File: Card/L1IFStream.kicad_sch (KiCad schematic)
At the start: 109 parts, among them J1 Conn_Coaxial, J2 USB_A, J3 RF_Shield_One_Piece, J4 Conn_Coaxial, U1 MAX2769BETI+T, U10 74LVC374, U11 74HC2GU04, U2 TPS717285DCK, U3 TPS717285DCK, U4 NCP164, U5 93LC66BT-I_OT, U6 FT2232H-Interface_USB, U7 74LVC1G74, U8 74LVC1G04, U9 74LVC374, X1 SIT5156, X2 SiT2024B, X3 QPQ1060

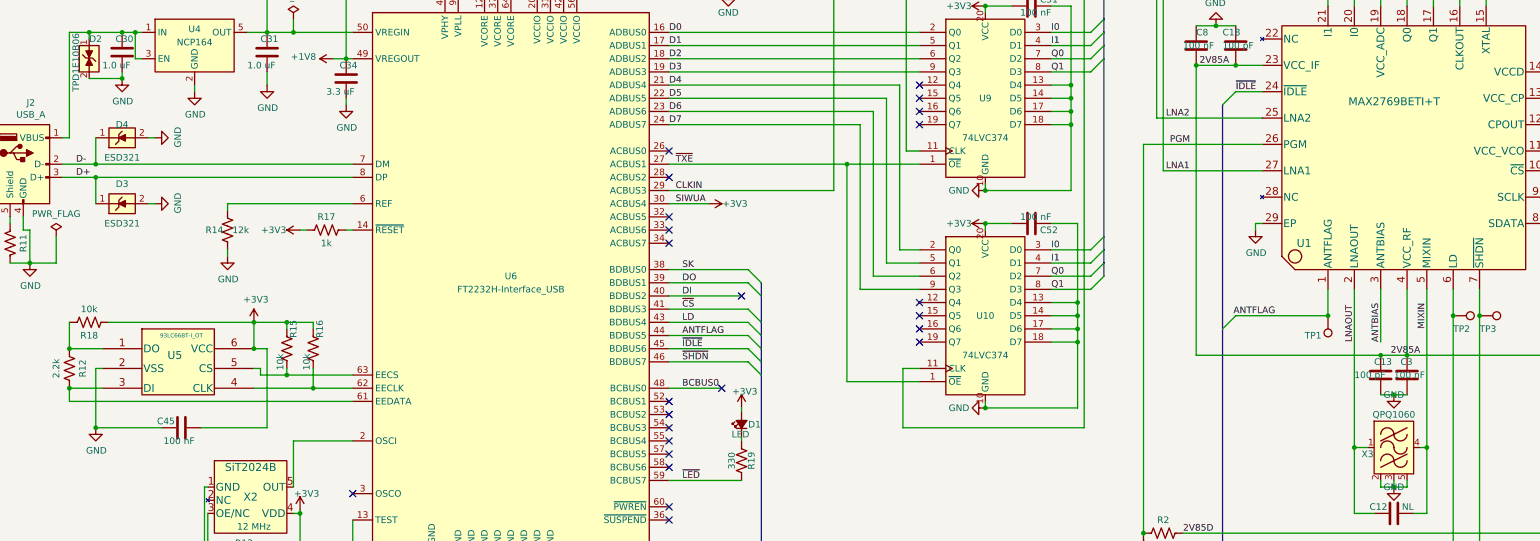
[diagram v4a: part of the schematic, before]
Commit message: Added SiTime 5156 16.367667 oscillator as alternate.
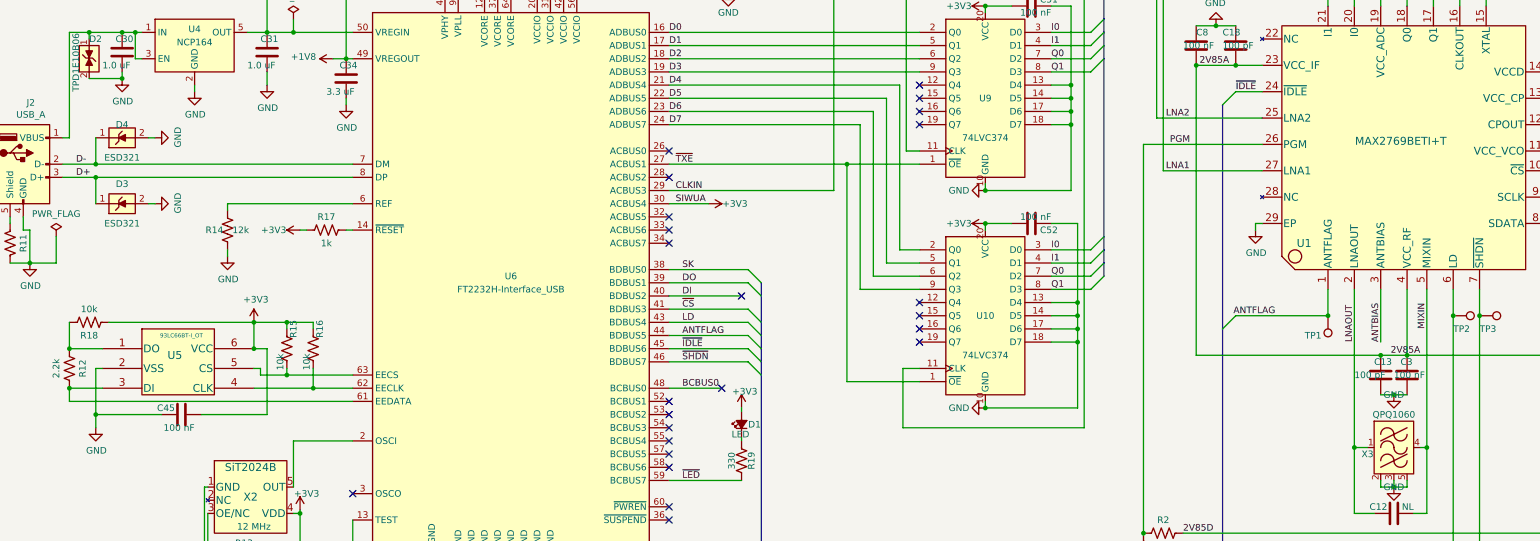
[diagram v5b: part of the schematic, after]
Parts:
- X1: MPN2 (none) -> SIT5156AICFK-30NO-16.367667; VPN2 (none) -> 1473-SIT5156AICFK-30N0-16.367667-ND
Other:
- moved on the sheet: C45
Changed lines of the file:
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@@
   (junction (at 29.21 123.19) (diameter 0) (color 0 0 0 0)
   )
-  (junction (at 34.29 138.43) (diameter 0) (color 0 0 0 0)
-  )
   (junction (at 401.32 139.7) (diameter 0) (color 0 0 0 0)
   )
@@
   (junction (at 223.52 22.86) (diameter 0) (color 0 0 0 0)
   )
+  (junction (at 34.29 135.89) (diameter 0) (color 0 0 0 0)
+  )
   (junction (at 82.55 67.31) (diameter 0) (color 0 0 0 0)
   )
@@
     (stroke (width 0) (type default))
   )
+  (wire (pts (xy 67.31 123.19) (xy 67.31 135.89))
+    (stroke (width 0) (type default))
+  )
   (wire (pts (xy 115.57 25.4) (xy 115.57 24.13))
     (stroke (width 0) (type default))
@@
     (stroke (width 0) (type default))
   )
-  (wire (pts (xy 54.61 138.43) (xy 67.31 138.43))
-    (stroke (width 0) (type default))
-  )
   (wire (pts (xy 205.74 92.71) (xy 205.74 91.44))
     (stroke (width 0) (type default))
@@
     (stroke (width 0) (type default))
   )
+  (wire (pts (xy 34.29 135.89) (xy 46.99 135.89))
+    (stroke (width 0) (type default))
+  )
   (wire (pts (xy 55.245 149.86) (xy 55.88 149.86))
     (stroke (width 0) (type default))
@@
     (stroke (width 0) (type default))
   )
+  (wire (pts (xy 34.29 135.89) (xy 34.29 138.43))
+    (stroke (width 0) (type default))
+  )
   (wire (pts (xy 193.04 22.86) (xy 193.04 35.56))
     (stroke (width 0) (type default))
@@
     (stroke (width 0) (type default))
   )
+  (wire (pts (xy 54.61 135.89) (xy 67.31 135.89))
+    (stroke (width 0) (type default))
+  )
   (wire (pts (xy 250.19 60.96) (xy 254 60.96))
     (stroke (width 0) (type default))
@@
     (stroke (width 0) (type default))
   )
-  (wire (pts (xy 46.99 138.43) (xy 34.29 138.43))
-    (stroke (width 0) (type default))
-  )
   (wire (pts (xy 360.68 53.34) (xy 360.68 54.61))
     (stroke (width 0) (type default))
@@
     (stroke (width 0) (type default))
   )
-  (wire (pts (xy 34.29 127) (xy 34.29 138.43))
+  (wire (pts (xy 34.29 127) (xy 34.29 135.89))
     (stroke (width 0) (type default))
   )
@@
     (stroke (width 0) (type default))
   )
-  (wire (pts (xy 67.31 138.43) (xy 67.31 123.19))
-    (stroke (width 0) (type default))
-  )
   (wire (pts (xy 127 53.34) (xy 127 52.07))
     (stroke (width 0) (type default))
@@
       (effects (font (size 1.524 1.524)) (justify left))
     )
-    (property "Value" "MAX2769BETI+T" (at 293.37 75.565 90)
+    (property "Value" "MAX2769BETI+T" (at 294.64 83.185 90)
       (effects (font (size 1.524 1.524)) (justify left))
     )
@@
     )
   )
-  (symbol (lib_id "L1IF:Capacitor") (at 50.8 138.43 90) (unit 1)
+  (symbol (lib_id "L1IF:Capacitor") (at 50.8 135.89 90) (unit 1)
     (in_bom yes) (on_board yes) (dnp no)
-    (property "Reference" "C45" (at 49.53 137.16 90)
+    (property "Reference" "C45" (at 49.53 134.62 90)
       (effects (font (size 1.27 1.27)) (justify left))
     )
-    (property "Value" "100 nF" (at 53.34 140.97 90)
+    (property "Value" "100 nF" (at 53.34 138.43 90)
       (effects (font (size 1.27 1.27)) (justify left))
     )
-    (property "Footprint" "L1IF:C_0402_1005Metric" (at 54.61 137.4648 0)
+    (property "Footprint" "L1IF:C_0402_1005Metric" (at 54.61 134.9248 0)
       (effects (font (size 1.27 1.27)) hide)
     )
-    (property "Datasheet" "~" (at 50.8 138.43 0)
+    (property "Datasheet" "~" (at 50.8 135.89 0)
       (effects (font (size 1.27 1.27)) hide)
     )
-    (property "Description" "CAP CER 0.1UF 16V X7R 0402 10%" (at 50.8 138.43 0)
+    (property "Description" "CAP CER 0.1UF 16V X7R 0402 10%" (at 50.8 135.89 0)
       (effects (font (size 1.27 1.27)) hide)
     )
-    (property "Manufacturer" "Murata Electronics" (at 50.8 138.43 0)
+    (property "Manufacturer" "Murata Electronics" (at 50.8 135.89 0)
       (effects (font (size 1.27 1.27)) hide)
     )
-    (property "MPN" "GRM155R71C104KA88J" (at 50.8 138.43 0)
+    (property "MPN" "GRM155R71C104KA88J" (at 50.8 135.89 0)
       (effects (font (size 1.27 1.27)) hide)
     )
-    (property "Vendor" "DigiKey" (at 50.8 138.43 0)
+    (property "Vendor" "DigiKey" (at 50.8 135.89 0)
       (effects (font (size 1.27 1.27)) hide)
     )
-    (property "Vendor PN" "490-6328-6-ND" (at 50.8 138.43 0)
+    (property "Vendor PN" "490-6328-6-ND" (at 50.8 135.89 0)
       (effects (font (size 1.27 1.27)) hide)
     )
@@
       (effects (font (size 1.27 1.27)))
     )
+    (property "MPN2" "SIT5156AICFK-30NO-16.367667" (at 328.93 40.64 0)
+      (effects (font (size 1.27 1.27)) hide)
+    )
+    (property "VPN2" "1473-SIT5156AICFK-30N0-16.367667-ND" (at 328.93 40.64 0)
+      (effects (font (size 1.27 1.27)) hide)
+    )
     (pin "6")
